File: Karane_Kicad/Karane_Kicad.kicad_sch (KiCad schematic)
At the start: 46 parts, among them J2 SerialWire, J3 FFC, J8 Conn_01x02_Socket, Q1 AO3400A, SW1 SW_Push, SW2 SW_Push, SW3 SW_Push, U19 STM32f103C8t6, U23 MPU6500, Y1 8Mhz

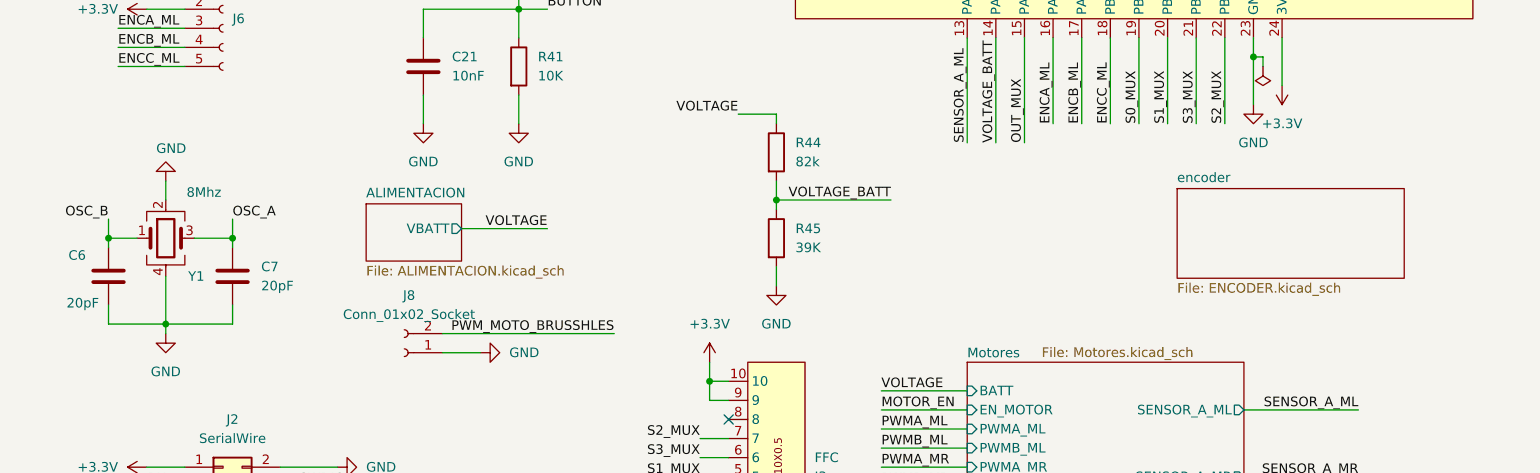
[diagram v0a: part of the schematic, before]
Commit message: Agregado Mosfet dual
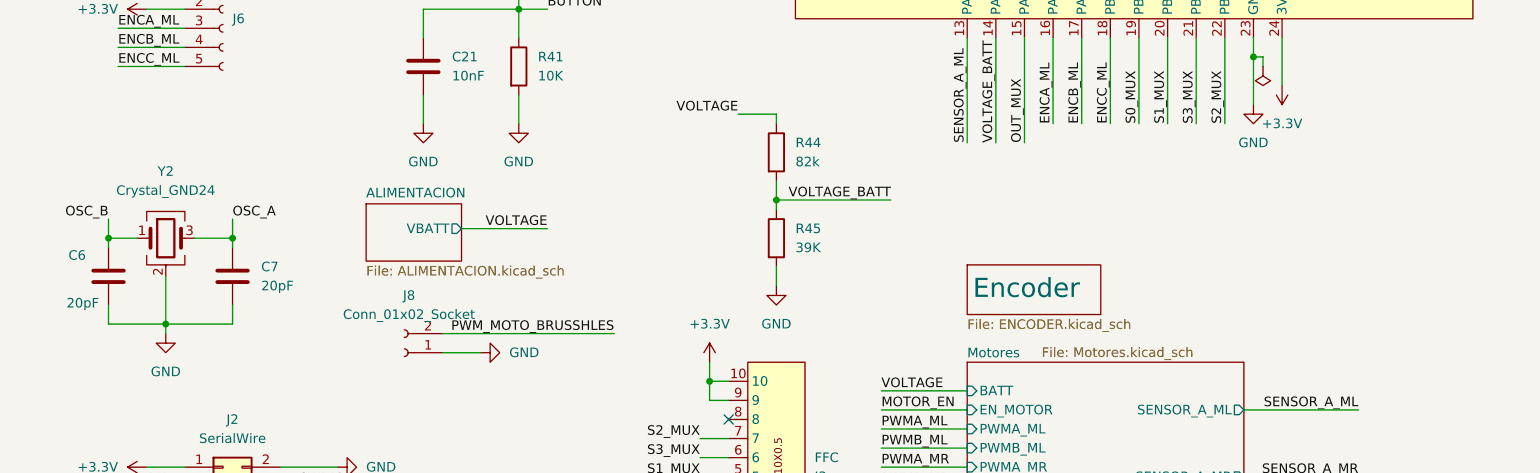
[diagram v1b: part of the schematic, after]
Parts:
- removed Y1: 8Mhz, Crystal:Crystal_SMD_3225-4Pin_3.2x2.5mm, symbol Device:Crystal_GND24
- added Y2: Crystal_GND24, Crystal:Crystal_SMD_3225-4Pin_3.2x2.5mm, symbol Device:Crystal_GND24
- J6, J7: value ~ -> (none)
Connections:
- net GND: now also Y2.2 (G), Y2.4 (G)
- net OSC_A: now also Y2.3
- net OSC_B: now also Y2.1
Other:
- sheet encoder renamed Encoder

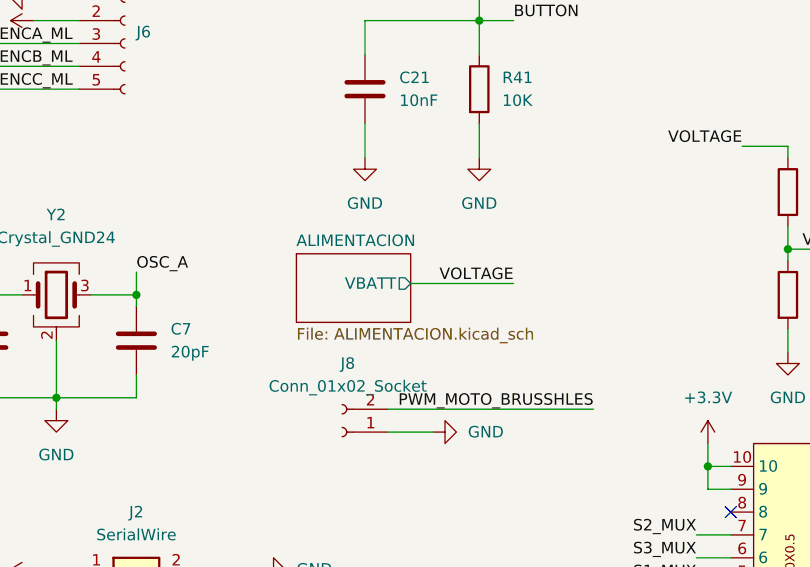
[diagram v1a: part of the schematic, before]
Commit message: Agregado symbol de mosfet
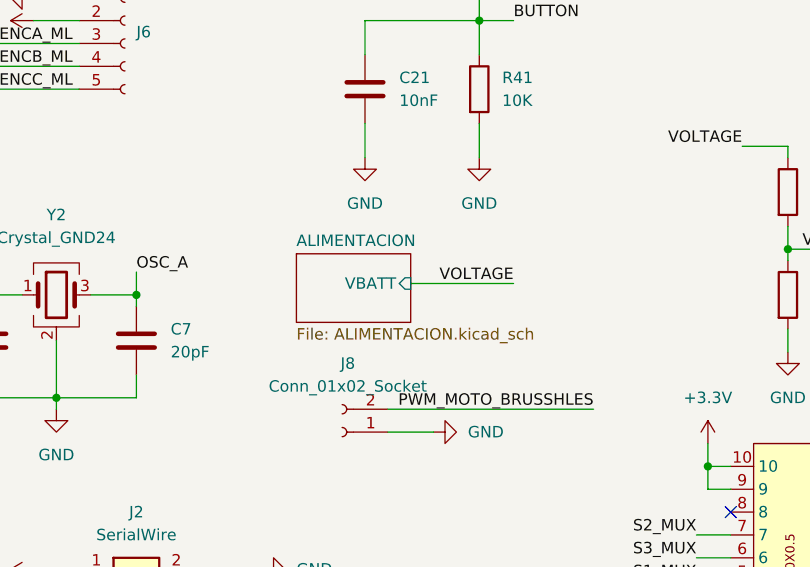
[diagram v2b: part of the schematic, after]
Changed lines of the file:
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@@
 			)
 		)
-		(pin "VBATT" output
+		(pin "VBATT" input
 			(at 71.12 118.11 0)
 			(effects

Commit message: Cambio de f103 a f401
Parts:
- removed R35: 100K, Resistor_SMD:R_0805_2012Metric_Pad1.20x1.40mm_HandSolder, symbol Device:R
- removed U19: STM32f103C8t6, Package_QFP:LQFP-48_7x7mm_P0.5mm, symbol Micromouse_Library:STM32F103C8T6
- added C16, C5: 4.7uF, Capacitor_SMD:C_0603_1608Metric_Pad1.08x0.95mm_HandSolder, symbol Device:C
- added C17: 1uF, Capacitor_SMD:C_0603_1608Metric_Pad1.08x0.95mm_HandSolder, symbol Device:C
- added C2: 10nF, Capacitor_SMD:C_0603_1608Metric_Pad1.08x0.95mm_HandSolder, symbol Device:C
- added D1: Inolux_IN-P55TATRGB, LED_SMD:LED_Inolux_IN-P55TATRGB_PLCC6_5.0x5.5mm_P1.8mm, symbol LED:Inolux_IN-P55TATRGB
- added D7: LED, LED_SMD:LED_1206_3216Metric_Pad1.42x1.75mm_HandSolder, symbol Device:LED
- added D8: SS34, Diode_SMD:D_SMA, symbol Diode:SS34
- added J2: (no value), Footprint:usb_C_stm32, symbol Micromouse_Library:USB_C_SW_UART_CONECTOR
- added J7: Motor_8520, Connector_PinHeader_2.54mm:PinHeader_1x02_P2.54mm_Vertical, symbol Connector:Conn_01x02_Socket
- added Q2: AO3400A, Package_TO_SOT_SMD:SOT-23, symbol Transistor_FET:AO3400A
- added R10, R18, R8, R9: 220, Resistor_SMD:R_0805_2012Metric_Pad1.20x1.40mm_HandSolder, symbol Device:R
- added R19: 10k, Resistor_SMD:R_0805_2012Metric_Pad1.20x1.40mm_HandSolder, symbol Device:R
- added R3, R4: 10K, Resistor_SMD:R_0805_2012Metric_Pad1.20x1.40mm_HandSolder, symbol Device:R
- added R5: 100, Resistor_SMD:R_0805_2012Metric_Pad1.20x1.40mm_HandSolder, symbol Device:R
- added SW2: SW_Push, Button_Switch_SMD:SW_SPST_CK_RS282G05A3, symbol Switch:SW_Push
- added U1: vs1838, Connector_PinHeader_2.54mm:PinHeader_1x03_P2.54mm_Vertical, symbol Micromouse_Library:1838
- added U2: (no value), Package_QFP:LQFP-64_10x10mm_P0.5mm, symbol Micromouse_Library:STM32F401RCT6
- renumbered C8 to C1, C24 to C10, C13 to C11, C14 to C12, C12 to C13, C10 to C14, C11 to C15, C21 to C3, C9 to C4, C22 to C6, C6 to C7, C23 to C8, C7 to C9, D1 to D2, D2 to D3, D3 to D4, D4 to D5, D5 to D6, J3 to J1, J2 to J3, J6 to J4, J7 to J5, J8 to J6, R40 to R1, R46 to R11, R47 to R12, R48 to R13, R49 to R14, R44 to R15, R45 to R16, R50 to R17, R34 to R2, R41 to R6, R36 to R7, SW2 to SW4, U23 to U3, Y2 to Y1
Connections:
- net +3.3V: now also C16.1, C17.1, J2.11 (VCC), J2.2 (VCC), R4.1, R5.1, SW2.1, U2.1 (VBAT), U2.13 (VDDA/VREF++), U2.19 (VDD), U2.32 (VDD), U2.48 (VDD), U2.64 (VDD)
- net BOOT0: now also U2.60 (BOOT0)
- net ENCA_ML: now also U2.14 (PA0)
- net ENCA_MR: now also U2.21 (PA5)
- net ENCB_ML: now also U2.15 (PA1)
- net ENCB_MR: now also U2.55 (PB3)
- net ENCC_ML: now also U2.16 (PA2)
- net ENCC_MR: now also U2.54 (PD2)
- net EN_SENSORES: now also U2.56 (PB4)
- net GND: now also C16.2, C17.2, C2.2, C5.2, D1.1 (KB), D1.2 (KR), D1.3 (KG), J2.1 (GND), J2.12 (GND), J2.13 (SHIELD), Q2.2 (S), R18.2, R19.2, R3.2, U1.2 (gnd), U2.12 (VSSA/VREF---), U2.18 (VSS), U2.31 (VSS), U2.47 (VSS), U2.63 (VSS)
- net LED1: now also U2.36 (PB15)
- net LED2: now also U2.35 (PB14)
- net LED3: now also U2.34 (PB13)
- net LED4: now also U2.33 (PB12)
- net MISO: now also U2.52 (PC11)
- net MOSI: now also U2.53 (PC12)
- net MOTOR_EN: now also U2.57 (PB5)
- net NRST: now also U2.7 (NRST)
- net OSC_A: now also U2.5 (PH0/OSC_IN)
- net OSC_B: now also U2.6 (PH1/OSC_OUT)
- net OUT_MUX: now also U2.11 (PC3)
- net PWMA_ML: now also U2.62 (PB9)
- net PWMA_MR: now also U2.59 (PB7)
- net PWMB_ML: now also U2.61 (PB8)
- net PWMB_MR: now also U2.58 (PB6)
- net PWM_MOTO_BRUSSHLES: now also Q2.1 (G), R19.1, U2.41 (PA8)
- net RX: now also J2.10 (RX), J2.3 (RX), U2.38 (PC7)
- net S0_MUX: now also U2.24 (PC4)
- net S1_MUX: now also U2.25 (PC5)
- net S2_MUX: now also U2.26 (PB0)
- net S3_MUX: now also U2.27 (PB1)
- net SCK: now also U2.51 (PC10)
- net SENSOR_A_ML: now also U2.8 (PC0)
- net SENSOR_A_MR: now also U2.9 (PC1)
- net SS: now also U2.50 (PA15)
- net SWCLK: now also J2.5 (SWCLK), J2.8 (SWCLK), U2.49 (PA14)
- net SWDIO: now also J2.6 (SWDIO), J2.7 (SWDIO), U2.46 (PA13)
- net TX: now also J2.4 (TX), J2.9 (TX), U2.37 (PC6)
- net VOLTAGE: now also D8.1 (K), J7.1 (Pin_1)
- net VOLTAGE_BATT: now also U2.10 (PC2)
- net BUTTON renamed BUTTON_START
- net BUTTON_START: now also U2.28 (PB2/BOOT1)
- net LED5 renamed LED_OK
- net LED_OK: now also U2.40 (PC9)
- new net: C5.1, U2.30 (VCAP1)
- new net: D1.6 (AB), R10.1
- new net: D7.1 (K), R18.1
- new net: D8.2 (A), J7.2 (Pin_2), Q2.3 (D)
- new net: R5.2, U1.3 (vcc)
- new net: D1.5 (AR), R9.1
- new net: D1.4 (AG), R8.1
- new net BUTTON_STOP: C2.1, R3.1, SW2.2, U2.29 (PB10)
- new net IR_36KHZ: R4.2, U1.1 (out), U2.45 (PA12)
- new net LED_ALARMA: D7.2 (A), U2.39 (PC8)
- new net PWM_BLUE: R10.2, U2.44 (PA11)
- new net PWM_GREEN: R8.2, U2.43 (PA10)
- new net PWM_RED: R9.2, U2.42 (PA9)
- no-connect marks 6 -> 13
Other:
- moved on the sheet: C10, C11, C12, C13, C14, C15, C6, C7, C8, C9, D2, D3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

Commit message: planos de alimentacion hechos
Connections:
- net +3.3V: no longer C10.1, C11.1, C12.1, C13.1, C14.1, C15.1, C16.1, C17.1, C6.1, J2.11 (VCC), J2.2 (VCC), J3.1 (Pin_1), J4.2, U2.1 (VBAT), U2.13 (VDDA/VREF++), U2.19 (VDD), U2.32 (VDD), U2.48 (VDD), U2.64 (VDD), U3.13 (VDD), U3.8 (VDDIO)
- new net +3.3VA: C10.1, C11.1, C12.1, C13.1, C14.1, C15.1, C16.1, C17.1, C6.1, J2.11 (VCC), J2.2 (VCC), J3.1 (Pin_1), J4.2, U2.1 (VBAT), U2.13 (VDDA/VREF++), U2.19 (VDD), U2.32 (VDD), U2.48 (VDD), U2.64 (VDD), U3.13 (VDD), U3.8 (VDDIO)

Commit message: mitada de componentes colocados
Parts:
- added C44: 100nF, Capacitor_SMD:C_0603_1608Metric_Pad1.08x0.95mm_HandSolder, symbol Device:C
- SW1, SW2, SW3, SW4: footprint Button_Switch_SMD:SW_SPST_CK_RS282G05A3 -> Button_Switch_SMD:SW_Push_SPST_NO_Alps_SKRK
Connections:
- net BUTTON_START: now also U2.57 (PB5); no longer U2.28 (PB2/BOOT1)
- net BUTTON_STOP: now also U2.56 (PB4); no longer U2.29 (PB10)
- net ENCA_ML: now also U2.21 (PA5); no longer U2.14 (PA0)
- net ENCA_MR: now also U2.14 (PA0); no longer U2.21 (PA5)
- net ENCB_ML: now also U2.55 (PB3); no longer U2.15 (PA1)
- net ENCB_MR: now also U2.15 (PA1); no longer U2.55 (PB3)
- net ENCC_ML: now also U2.54 (PD2); no longer U2.16 (PA2)
- net ENCC_MR: now also U2.16 (PA2); no longer U2.54 (PD2)
- net EN_SENSORES: now also U2.23 (PA7); no longer U2.56 (PB4)
- net GND: now also C44.2
- net MOTOR_EN: now also U2.22 (PA6); no longer U2.57 (PB5)
- net OSC_A: now also C7.1, Y1.1; no longer C9.1, Y1.3
- net OSC_B: now also C9.1, Y1.3; no longer C7.1, Y1.1
- net PWMA_ML: now also U2.59 (PB7); no longer U2.62 (PB9)
- net PWMA_MR: now also U2.62 (PB9); no longer U2.59 (PB7)
- net PWMB_ML: now also U2.58 (PB6); no longer U2.61 (PB8)
- net PWMB_MR: now also U2.61 (PB8); no longer U2.58 (PB6)
- net S2_MUX: now also U2.27 (PB1); no longer U2.26 (PB0)
- net S3_MUX: now also U2.26 (PB0); no longer U2.27 (PB1)
- net SENSOR_A_ML: now also U2.9 (PC1); no longer U2.8 (PC0)
- net SENSOR_A_MR: now also U2.8 (PC0); no longer U2.9 (PC1)
- net VOLTAGE_BATT: now also C44.1

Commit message: finalizado pcb v2
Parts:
- removed J3: SerialWire, Connector_IDC:IDC-Header_2x03_P2.54mm_Vertical, symbol Connector_Generic:Conn_02x03_Odd_Even
- J4, J5: footprint Footprint:as5145_con_1.27 -> Footprint:AS5145_CONN_PCB
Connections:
- net +3.3V: now also J4.2; no longer J5.2, R2.1, R4.1, R5.1, SW2.1, SW3.1, SW4.1
- net +3.3VA: now also J5.2, R2.1, R4.1, R5.1, SW2.1, SW3.1, SW4.1; no longer J4.2
- net GND: now also R10.2, R8.2, R9.2; no longer D1.1 (KB), D1.2 (KR), D1.3 (KG)
- net PWM_BLUE: now also D1.4 (AG); no longer R10.2
- net PWM_GREEN: now also D1.5 (AR); no longer R8.2
- net PWM_RED: now also D1.6 (AB); no longer R9.2
- net at R10.1: now also D1.3 (KG); no longer D1.6 (AB)
- net at R9.1: now also D1.2 (KR); no longer D1.5 (AR)
- net at R8.1: now also D1.1 (KB); no longer D1.4 (AG)
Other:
- moved on the sheet: D1, R10, R8, R9

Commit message: Agregado agujeros a pcb
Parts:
- added H5, H6, H7, H8: MountingHole_Pad, MountingHole:MountingHole_2.2mm_M2_ISO14580_Pad, symbol Mechanical:MountingHole_Pad
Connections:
- net GND: now also H5.1, H6.1, H7.1, H8.1
